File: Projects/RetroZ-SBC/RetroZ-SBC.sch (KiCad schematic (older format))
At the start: 58 parts, among them IC1 PO_RESET, IC2 AT28C256B-15PU, IC3 AS6C62256-55PCN, J1 02x20, J2 01x08, J3 01x08, J4 PARENT INT. SEL., J5 USB_OTG, J6 CLOCK DIV., J7 PSW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

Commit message: added a dip switch to toggle the computer power
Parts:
- removed J7: PSW, Pin_Headers:Pin_Header_Straight_1x02_Pitch2.54mm, symbol Connector_Generic:Conn_01x02
- added SW2: POWER SWITCH, Buttons_Switches_THT:SW_DIP_x1_W7.62mm_Slide, symbol Switch:SW_DIP_x01
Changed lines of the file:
@@
 EESchema Schematic File Version 4
-LIBS:RetroZ-SBC-cache
 EELAYER 26 0
 EELAYER END
@@
 L power:PWR_FLAG #FLG01
 U 1 1 5C206B07
-P 10325 1350
-F 0 "#FLG01" H 10325 1425 50  0001 C CNN
-F 1 "PWR_FLAG" V 10325 1478 50  0000 L CNN
-F 2 "" H 10325 1350 50  0001 C CNN
-F 3 "~" H 10325 1350 50  0001 C CNN
-	1    10325 1350
-	0    -1   -1   0
+P 10925 1475
+F 0 "#FLG01" H 10925 1550 50  0001 C CNN
+F 1 "PWR_FLAG" V 10925 1603 50  0000 L CNN
+F 2 "" H 10925 1475 50  0001 C CNN
+F 3 "~" H 10925 1475 50  0001 C CNN
+	1    10925 1475
+	0    1    1    0
 $EndComp
 $Comp
@@
 L power:VCC #PWR021
 U 1 1 5C44B15F
-P 10325 1275
-F 0 "#PWR021" H 10325 1125 50  0001 C CNN
-F 1 "VCC" H 10342 1448 50  0000 C CNN
-F 2 "" H 10325 1275 50  0001 C CNN
-F 3 "" H 10325 1275 50  0001 C CNN
-	1    10325 1275
+P 10925 1425
+F 0 "#PWR021" H 10925 1275 50  0001 C CNN
+F 1 "VCC" H 10942 1598 50  0000 C CNN
+F 2 "" H 10925 1425 50  0001 C CNN
+F 3 "" H 10925 1425 50  0001 C CNN
+	1    10925 1425
 	-1   0    0    -1
 $EndComp
@@
 Text Label 12900 3725 2    50   ~ 0
 ~WAIT
-$Comp
-L Connector_Generic:Conn_01x02 J7
-U 1 1 5C2BA53D
-P 10525 1525
-F 0 "J7" H 10444 1200 50  0000 C CNN
-F 1 "PSW" H 10444 1291 50  0000 C CNN
-F 2 "Pin_Headers:Pin_Header_Straight_1x02_Pitch2.54mm" H 10525 1525 50  0001 C CNN
-F 3 "~" H 10525 1525 50  0001 C CNN
-	1    10525 1525
-	1    0    0    1
-$EndComp
-Connection ~ 10325 1350
-Wire Wire Line
-	10325 1350 10325 1425
-Wire Wire Line
-	10325 1525 10325 1650
-Wire Wire Line
-	10325 1275 10325 1350
 Wire Wire Line
 	6275 5275 6800 5275
@@
 Wire Wire Line
 	8475 7975 8800 7975
+Text Notes 8900 8400 0    50   ~ 0
+NOTE:\nWhen MEM_EXT is HIGH, \nthe onboard memory is \ndisabled. Otherwise, this \npin shall stay floating.
+$Comp
+L Switch:SW_DIP_x01 SW2
+U 1 1 5C306881
+P 10625 1575
+F 0 "SW2" H 10625 1308 50  0000 C CNN
+F 1 "POWER SWITCH" H 10625 1399 50  0000 C CNN
+F 2 "Buttons_Switches_THT:SW_DIP_x1_W7.62mm_Slide" H 10625 1575 50  0001 C CNN
+F 3 "" H 10625 1575 50  0001 C CNN
+	1    10625 1575
+	-1   0    0    1
+$EndComp
+Wire Wire Line
+	10925 1425 10925 1475
+Connection ~ 10925 1475
+Wire Wire Line
+	10925 1475 10925 1575
+Wire Wire Line
+	10325 1575 10325 1650
 Wire Wire Line
 	7325 8575 7825 8575
@@
 Wire Bus Line
 	3500 3425 3500 6500
-Text Notes 8900 8400 0    50   ~ 0
-NOTE:\nWhen MEM_EXT is HIGH, \nthe onboard memory is \ndisabled. Otherwise, this \npin shall stay floating.
 $EndSCHEMATC

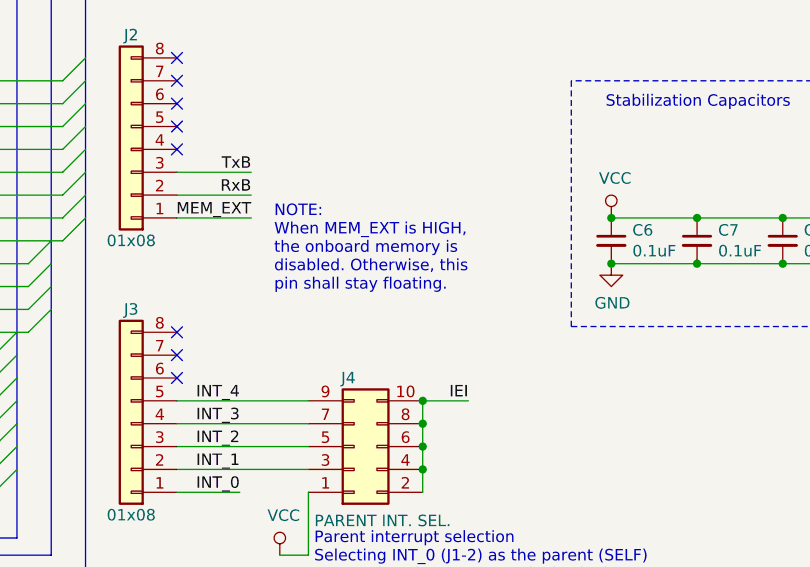
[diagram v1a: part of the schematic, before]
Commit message: updated readme.md and some schematic texts
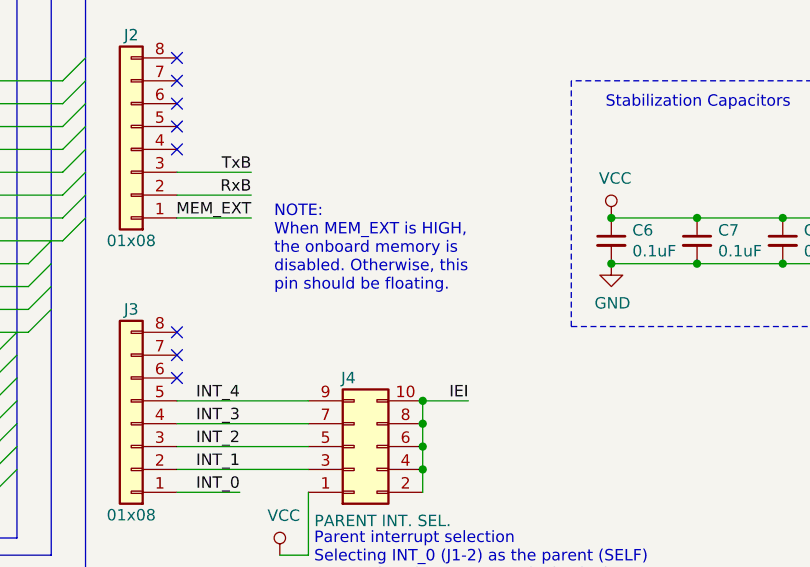
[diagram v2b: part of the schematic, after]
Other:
- note added: "NOTE:\nWhen MEM_EXT is HIGH, \nthe onboard memory is \ndisabled. Otherwise, this \npin should be floating."
- note removed: "NOTE:\nWhen MEM_EXT is HIGH, \nthe onboard memory is \ndisabled. Otherwise, this \npin shall stay floating."
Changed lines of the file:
@@
 EESchema Schematic File Version 4
+LIBS:RetroZ-SBC-cache
 EELAYER 26 0
 EELAYER END
@@
 	8475 7975 8800 7975
 Text Notes 8900 8400 0    50   ~ 0
-NOTE:\nWhen MEM_EXT is HIGH, \nthe onboard memory is \ndisabled. Otherwise, this \npin shall stay floating.
+NOTE:\nWhen MEM_EXT is HIGH, \nthe onboard memory is \ndisabled. Otherwise, this \npin should be floating.
 $Comp
 L Switch:SW_DIP_x01 SW2

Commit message: moved some high speed signals traces away from other traces
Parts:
- J2: value 01x08 -> User Port A
- J3: value 01x08 -> User Port B
- J4: value PARENT INT. SEL. -> IEI SELECT
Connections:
- wire segments 323 -> 324
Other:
- note added: "DUAL SERIAL IO DEVICE \nINTERRUPT 0 (INT_0)\nDEVICE PORTS 0x00 to 0x03\n==================\n0x00: Channel A, Control\n0x01: Channel A, Data\n0x02: Channel B, Control\n0x03: Channel B, Data"
- note removed: "DUAL SERIAL IO DEVICE \nINTERRUPT 0 (INT_0)\nDEVICE PORTS 0x00 to 0x03\n========================\n0x00 (00000000): Channel A, Control\n0x01 (00000001): Channel A, Data\n0x02 (00000010): Channel B, Control\n0x03 (00000011): Channel B, Data"
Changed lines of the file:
@@
 ~INT
-Wire Wire Line
-	11100 5525 11000 5525
-Wire Wire Line
-	11000 5525 11000 5675
 Wire Wire Line
 	11100 4925 10925 4925
@@
 	11100 4125 10775 4125
 Text Notes 11250 6400 0    50   ~ 0
-DUAL SERIAL IO DEVICE \nINTERRUPT 0 (INT_0)\nDEVICE PORTS 0x00 to 0x03\n========================\n0x00 (00000000): Channel A, Control\n0x01 (00000001): Channel A, Data\n0x02 (00000010): Channel B, Control\n0x03 (00000011): Channel B, Data
+DUAL SERIAL IO DEVICE \nINTERRUPT 0 (INT_0)\nDEVICE PORTS 0x00 to 0x03\n==================\n0x00: Channel A, Control\n0x01: Channel A, Data\n0x02: Channel B, Control\n0x03: Channel B, Data
 Wire Wire Line
 	10350 5425 10350 5500
@@
 P 8275 7775
 F 0 "J2" H 8275 7275 50  0000 C CNN
-F 1 "01x08" H 8275 8175 50  0000 C CNN
+F 1 "User Port A" H 8175 8175 50  0000 C CNN
 F 2 "Socket_Strips:Socket_Strip_Straight_1x08_Pitch2.54mm" H 8275 7775 50  0001 C CNN
 F 3 "~" H 8275 7775 50  0001 C CNN
@@
 P 8275 8975
 F 0 "J3" H 8275 8475 50  0000 C CNN
-F 1 "01x08" H 8275 9375 50  0000 C CNN
+F 1 "User Port B" H 8200 9375 50  0000 C CNN
 F 2 "Socket_Strips:Socket_Strip_Straight_1x08_Pitch2.54mm" H 8275 8975 50  0001 C CNN
 F 3 "~" H 8275 8975 50  0001 C CNN
@@
 Text Label 9750 8875 2    50   ~ 0
 IEI
-Wire Wire Line
-	9550 8875 9750 8875
 Text Label 8750 9175 2    50   ~ 0
 INT_1
@@
 Text Label 8750 9275 2    50   ~ 0
 INT_0
-Text Label 10875 5675 0    50   ~ 0
-IEI
-Wire Wire Line
-	10875 5675 11000 5675
 Text Notes 9075 9750 0    50   ~ 0
 Parent interrupt selection\nSelecting INT_0 (J1-2) as the parent (SELF)\nmeans that the current IO device is the \nfirst device of the dasy chain.
@@
 P 9250 9075
 F 0 "J4" H 9225 8775 50  0000 C CNN
-F 1 "PARENT INT. SEL." H 9375 9400 50  0000 C CNN
+F 1 "IEI SELECT" H 9300 9375 50  0000 C CNN
 F 2 "Pin_Headers:Pin_Header_Straight_2x05_Pitch2.54mm" H 9250 9075 50  0001 C CNN
 F 3 "~" H 9250 9075 50  0001 C CNN
@@
 	10325 1575 10325 1650
 Wire Wire Line
+	10650 7100 9950 7100
+Wire Wire Line
+	9950 7100 9950 8875
+Wire Wire Line
+	9550 8875 9950 8875
+Wire Wire Line
+	10650 5525 11100 5525
+Wire Wire Line
+	10650 5525 10650 7100
+Wire Wire Line
 	7325 8575 7825 8575

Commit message: added pull-up resistors and comments
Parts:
- added R13, R14: 10K, Resistors_THT:R_Axial_DIN0207_L6.3mm_D2.5mm_P10.16mm_Horizontal, symbol Device:R
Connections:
- wire segments 324 -> 331
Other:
- note added: "The ADM803TAKSZ-REEL7 chip is a \nlittle package that monitors the \npower line. When the device is \npowered, it pulls the ~RESET~ pin \nlow for 240ms then keep it open for\nas long as the device is powered. Still\nneed a pull-up resistor to keep ~RESET~\nhigh afterward."
- moved on the sheet: R3, R4, R5, R6, SW1

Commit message: moved interrupts to user port A
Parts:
- IC1: symbol SamacSys_Parts:ADM803TAKSZ-REEL7 -> RetroZ-SBC-rescue:ADM803TAKSZ-REEL7-SamacSys_Parts
- IC3: symbol SamacSys_Parts:AS6C62256-55PCN -> RetroZ-SBC-rescue:AS6C62256-55PCN-SamacSys_Parts
- J5: symbol Connector:USB_OTG -> RetroZ-SBC-rescue:USB_OTG-Connector
- U5: symbol Z84C40-SIO2:Z84C40 -> RetroZ-SBC-rescue:Z84C40-Z84C40-SIO2
- U6: symbol FT230XS-U:FT230XS-U -> RetroZ-SBC-rescue:FT230XS-U-FT230XS-U
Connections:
- wire segments 331 -> 328
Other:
- moved on the sheet: J4
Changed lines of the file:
@@
 $EndComp
 $Comp
-L SamacSys_Parts:AS6C62256-55PCN IC3
+L RetroZ-SBC-rescue:AS6C62256-55PCN-SamacSys_Parts IC3
 U 1 1 5C204B18
 P 8800 3325
@@
 $EndComp
 $Comp
-L SamacSys_Parts:ADM803TAKSZ-REEL7 IC1
+L RetroZ-SBC-rescue:ADM803TAKSZ-REEL7-SamacSys_Parts IC1
 U 1 1 5C5EAF92
 P 3050 2850
@@
 	3025 5750 3400 5750
 $Comp
-L Z84C40-SIO2:Z84C40 U5
+L RetroZ-SBC-rescue:Z84C40-Z84C40-SIO2 U5
 U 1 1 5C68DDF5
 P 11900 4375
@@
 Connection ~ 1575 5350
 $Comp
-L FT230XS-U:FT230XS-U U6
+L RetroZ-SBC-rescue:FT230XS-U-FT230XS-U U6
 U 1 1 5C2D1048
 P 12375 1775
@@
 $EndComp
 $Comp
-L Connector:USB_OTG J5
+L RetroZ-SBC-rescue:USB_OTG-Connector J5
 U 1 1 5C2DE828
 P 10025 1850
@@
 Text Label 8800 7875 2    50   ~ 0
 TxB
-NoConn ~ 8475 7375
-NoConn ~ 8475 7475
-NoConn ~ 8475 7575
-NoConn ~ 8475 7675
-NoConn ~ 8475 7775
 NoConn ~ 8475 8575
 NoConn ~ 8475 8675
@@
 L power:VCC #PWR019
 U 1 1 5D970B69
-P 8925 9550
-F 0 "#PWR019" H 8925 9400 50  0001 C CNN
-F 1 "VCC" H 8942 9723 50  0000 C CNN
-F 2 "" H 8925 9550 50  0001 C CNN
-F 3 "" H 8925 9550 50  0001 C CNN
-	1    8925 9550
-	1    0    0    -1
-$EndComp
-Wire Wire Line
-	9050 9275 9050 9550
-Wire Wire Line
-	9050 9550 8925 9550
-Wire Wire Line
-	9050 9175 8475 9175
-Wire Wire Line
-	8475 9075 9050 9075
-Wire Wire Line
-	9050 8975 8475 8975
-Text Label 9750 8875 2    50   ~ 0
+P 8950 7200
+F 0 "#PWR019" H 8950 7050 50  0001 C CNN
+F 1 "VCC" H 8967 7373 50  0000 C CNN
+F 2 "" H 8950 7200 50  0001 C CNN
+F 3 "" H 8950 7200 50  0001 C CNN
+	1    8950 7200
+	1    0    0    -1
+$EndComp
+Wire Wire Line
+	9050 7675 8475 7675
+Wire Wire Line
+	8475 7575 9050 7575
+Wire Wire Line
+	9050 7475 8475 7475
+Text Label 9750 7375 2    50   ~ 0
 IEI
-Text Label 8750 9175 2    50   ~ 0
+Text Label 8800 7675 2    50   ~ 0
 INT_1
-Text Label 8750 9075 2    50   ~ 0
+Text Label 8800 7575 2    50   ~ 0
 INT_2
-Text Label 8750 8975 2    50   ~ 0
+Text Label 8800 7475 2    50   ~ 0
 INT_3
-Text Label 8750 9275 2    50   ~ 0
+Text Label 8800 7775 2    50   ~ 0
 INT_0
-Text Notes 9075 9750 0    50   ~ 0
+Text Notes 9100 7200 0    50   ~ 0
 Parent interrupt selection\nSelecting INT_0 (J1-2) as the parent (SELF)\nmeans that the current IO device is the \nfirst device of the dasy chain.
 Wire Wire Line
-	8475 9275 8750 9275
-Wire Wire Line
-	9550 8975 9550 8875
-Connection ~ 9550 8975
-Wire Wire Line
-	9550 9075 9550 8975
-Connection ~ 9550 9075
-Wire Wire Line
-	9550 9175 9550 9075
-Wire Wire Line
-	9550 9275 9550 9175
-Connection ~ 9550 9175
-Connection ~ 9550 8875
+	9550 7475 9550 7375
+Connection ~ 9550 7475
+Wire Wire Line
+	9550 7575 9550 7475
+Connection ~ 9550 7575
+Wire Wire Line
+	9550 7675 9550 7575
+Wire Wire Line
+	9550 7775 9550 7675
+Connection ~ 9550 7675
 $Comp
 L Connector_Generic:Conn_02x05_Odd_Even J4
 U 1 1 5DA9A246
-P 9250 9075
-F 0 "J4" H 9225 8775 50  0000 C CNN
-F 1 "IEI SELECT" H 9300 9375 50  0000 C CNN
-F 2 "Pin_Headers:Pin_Header_Straight_2x05_Pitch2.54mm" H 9250 9075 50  0001 C CNN
-F 3 "~" H 9250 9075 50  0001 C CNN
-	1    9250 9075
+P 9250 7575
+F 0 "J4" H 9225 7275 50  0000 C CNN
+F 1 "IEI SELECT" H 9300 7875 50  0000 C CNN
+F 2 "Pin_Headers:Pin_Header_Straight_2x05_Pitch2.54mm" H 9250 7575 50  0001 C CNN
+F 3 "~" H 9250 7575 50  0001 C CNN
+	1    9250 7575
 	1    0    0    1
 $EndComp
 Wire Wire Line
-	9050 8875 8475 8875
-Text Label 8750 8875 2    50   ~ 0
+	9050 7375 8475 7375
+Text Label 8800 7375 2    50   ~ 0
 INT_4
 Text Notes 10350 7600 0    50   ~ 0
@@
 Wire Wire Line
 	8475 7975 8800 7975
-Text Notes 8900 8400 0    50   ~ 0
+Text Notes 8825 8400 0    50   ~ 0
 NOTE:\nWhen MEM_EXT is HIGH, \nthe onboard memory is \ndisabled. Otherwise, this \npin should be floating.
 $Comp
@@
 Wire Wire Line
 	10325 1575 10325 1650
-Wire Wire Line
-	10650 7100 9950 7100
-Wire Wire Line
-	9950 7100 9950 8875
-Wire Wire Line
-	9550 8875 9950 8875
-Wire Wire Line
-	10650 5525 11100 5525
-Wire Wire Line
-	10650 5525 10650 7100
 Text Notes 2975 2500 0    50   ~ 0
 The ADM803TAKSZ-REEL7 chip is a \nlittle package that monitors the \npower line. When the device is \npowered, it pulls the ~RESET~ pin \nlow for 240ms then keep it open for\nas long as the device is powered. Still\nneed a pull-up resistor to keep ~RESET~\nhigh afterward.
@@
 ~BUSACK
 Wire Wire Line
+	9750 7375 9550 7375
+Connection ~ 9550 7375
+Text Label 11000 5525 0    50   ~ 0
+IEI
+Wire Wire Line
+	11100 5525 11000 5525
+Wire Wire Line
+	9050 7775 8950 7775
+Wire Wire Line
+	8950 7775 8950 7200
+Wire Wire Line
+	8475 7775 8800 7775
+NoConn ~ 8475 8875
+NoConn ~ 8475 8975
+NoConn ~ 8475 9075
+NoConn ~ 8475 9175
+NoConn ~ 8475 9275
+Wire Wire Line
 	7325 8575 7825 8575

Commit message: added missing pull-ups and changed git status
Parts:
- J2, J3: footprint Socket_Strips:Socket_Strip_Straight_1x08_Pitch2.54mm -> Pin_Headers:Pin_Header_Straight_1x08_Pitch2.54mm
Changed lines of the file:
@@
 F 0 "J2" H 8275 7275 50  0000 C CNN
 F 1 "User Port A" H 8175 8175 50  0000 C CNN
-F 2 "Socket_Strips:Socket_Strip_Straight_1x08_Pitch2.54mm" H 8275 7775 50  0001 C CNN
+F 2 "Pin_Headers:Pin_Header_Straight_1x08_Pitch2.54mm" H 8275 7775 50  0001 C CNN
 F 3 "~" H 8275 7775 50  0001 C CNN
 	1    8275 7775
@@
 F 0 "J3" H 8275 8475 50  0000 C CNN
 F 1 "User Port B" H 8200 9375 50  0000 C CNN
-F 2 "Socket_Strips:Socket_Strip_Straight_1x08_Pitch2.54mm" H 8275 8975 50  0001 C CNN
+F 2 "Pin_Headers:Pin_Header_Straight_1x08_Pitch2.54mm" H 8275 8975 50  0001 C CNN
 F 3 "~" H 8275 8975 50  0001 C CNN
 	1    8275 8975

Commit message: added BOM information
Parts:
- C1, C2: Mfr# (none) -> C317C200J5G5TA
- C10, C11, C12, C5, C6, C7, C8, C9: Mfr# (none) -> C322C104K5R5TA7301
- C3, C4: Mfr# (none) -> FG28C0G1H470JNT06
- D1: Mfr# (none) -> 151051VS04000
- D2, D3: Mfr# (none) -> 151031SS06000
- IC1: Manufacturer_Part_Number ADM803TAKSZ-REEL7 -> (none); Mfr# (none) -> ADM803TAKSZ-REEL7
- IC2: Description AT28C64B-15PU, Parallel EEPROM Memory 64kbit, Parallel, 150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 -> AT28C256B-15PU, Parallel EEPROM Memory 256kbit, Parallel, 1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; Manufacturer_Part_Number AT28C64B-15PU -> (none); Mfr# (none) -> AT28C256-15PU; Mouser Part Number 556-AT28C64B15PU -> 556-AT28C25615PU
- IC3: Manufacturer_Part_Number AS6C62256-55PCN -> (none); Mfr# (none) -> AS6C62256-55PCN
- J1: Mfr# (none) -> 2223
- J4: Mfr# (none) -> PRPC005DAAN-RC; Mfr#2 (none) -> QPC02SXGN-RC
- J5: Mfr# (none) -> 629105150521
- J6: Mfr# (none) -> PRPC004DAAN-RC; Mfr#2 (none) -> QPC02SXGN-RC
- R1: Mfr# (none) -> RNF14FTD1M00
- R10, R11: Mfr# (none) -> RNF14FTD330R
- R12, R13, R14, R3, R4, R5, R6: Mfr# (none) -> RNF14FTD10K0
- R2: Mfr# (none) -> RNF14FTD1K00
- R7: Mfr# (none) -> RNF14FTD221R
- R8, R9: Mfr# (none) -> RNF14FTD27R4
- SW1: Mfr# (none) -> MJTP1230
- SW2: Mfr# (none) -> BD01
- U1: Mfr# (none) -> 74LS32
- U2: Mfr# (none) -> 74HCT04
- U3: Mfr# (none) -> Z84C0008PEG; Mfr#2 (none) -> 4840-6004-CP
- U4: Mfr# (none) -> SN74LS138N
- U5: Mfr# (none) -> Z84C4208PEG; Mfr#2 (none) -> 4840-6004-CP
- U6: Mfr# (none) -> FT230XS-U
- U7: Mfr# (none) -> 74LS92
- Y1: Mfr# (none) -> ECS-73-20-5PX-TR

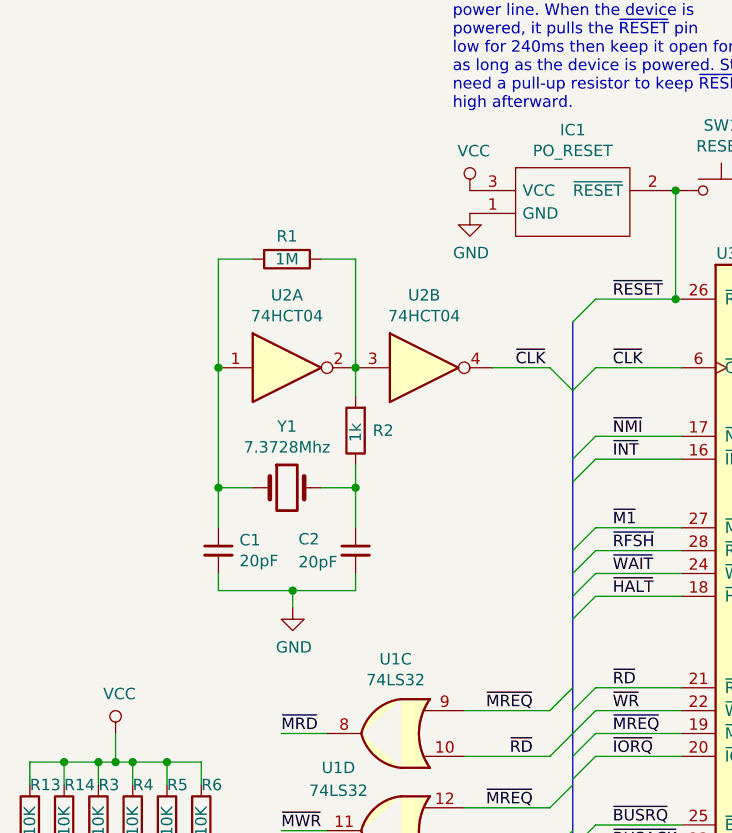
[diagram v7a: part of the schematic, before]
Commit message: added the S80 Library
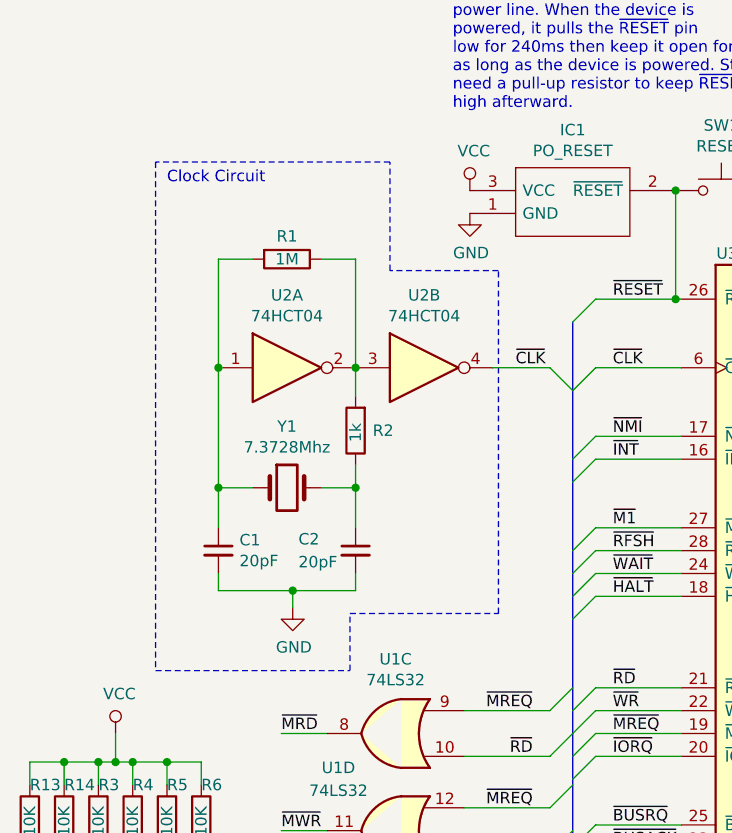
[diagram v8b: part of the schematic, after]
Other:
- note added: "Clock Circuit"
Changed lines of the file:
@@
 NoConn ~ 8475 9175
 NoConn ~ 8475 9275
+Wire Notes Line
+	1675 4950 2525 4950
+Wire Notes Line
+	2525 4950 2525 4700
+Wire Notes Line
+	2525 4700 3175 4700
+Wire Notes Line
+	3175 4700 3175 3200
+Wire Notes Line
+	3175 3200 2700 3200
+Wire Notes Line
+	2700 3200 2700 2725
+Wire Notes Line
+	2700 2725 1675 2725
 Wire Wire Line
 	7325 8575 7825 8575
 Wire Wire Line
 	7325 8175 7975 8175
+Wire Notes Line
+	1675 2725 1675 4950
 Wire Bus Line
 	7925 5925 7925 9550
@@
 Wire Bus Line
 	8475 2900 8475 6650
+Text Notes 1725 2825 0    50   ~ 0
+Clock Circuit
 $EndSCHEMATC
